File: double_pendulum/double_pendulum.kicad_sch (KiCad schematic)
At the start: 3 parts, among them J1 Conn_01x21_Socket, J2 Conn_01x21_Socket, U1 SC0915

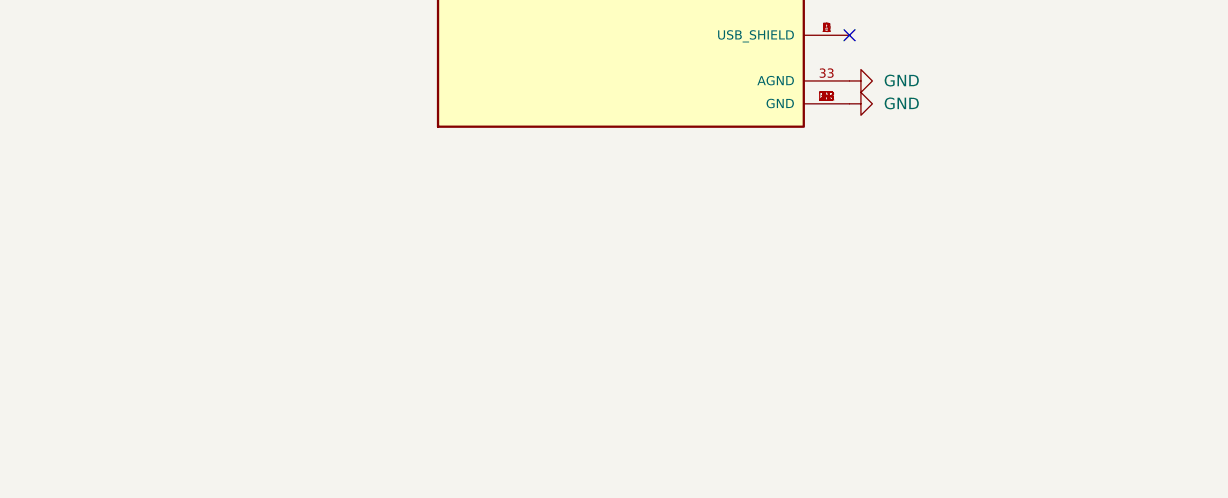
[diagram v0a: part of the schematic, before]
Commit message: Updated double pendulum with todo notes
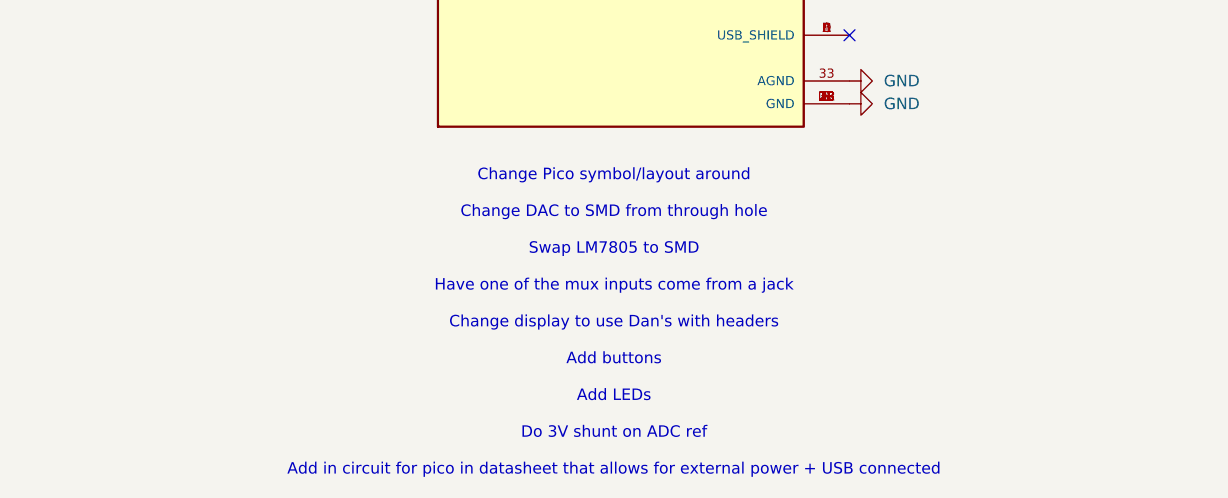
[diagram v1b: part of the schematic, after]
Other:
- note added: "Change Pico symbol/layout around Change DAC to SMD from through hole Swap LM7805 to SMD Have one of the mux inputs come from a jack Change display to use Dan's with headers Add buttons Add LEDs Do 3V shunt on ADC ref Add in circuit for pico in datasheet that allows for external power + USB connected"
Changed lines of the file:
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@@
 		(at 144.78 97.79)
+	)
+	(text "Change Pico symbol/layout around\n\nChange DAC to SMD from through hole\n\nSwap LM7805 to SMD\n\nHave one of the mux inputs come from a jack\n\nChange display to use Dan's with headers\n\nAdd buttons\n\nAdd LEDs\n\nDo 3V shunt on ADC ref\n\nAdd in circuit for pico in datasheet that allows for external power + USB connected "
+		(exclude_from_sim no)
+		(at 118.618 129.794 0)
+		(effects
+			(font
+				(size 1.27 1.27)
+			)
+		)
 	)
 	(global_label "SCL_DISPLAY"

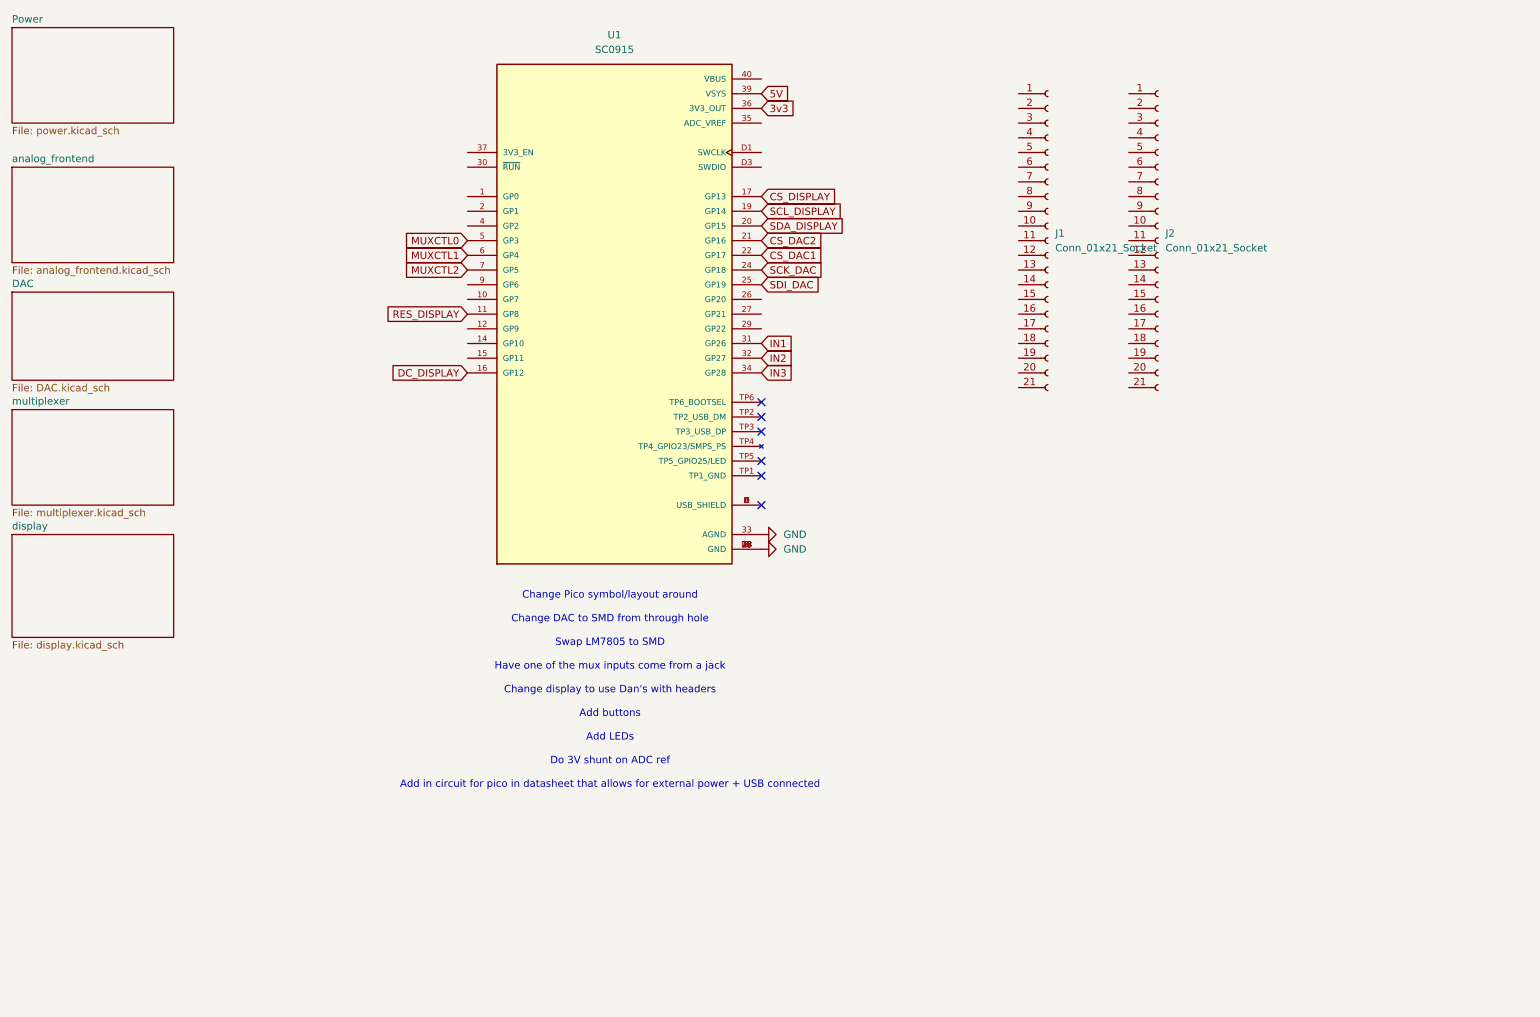
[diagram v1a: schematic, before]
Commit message: Finished schematic and layout of the double pendulum
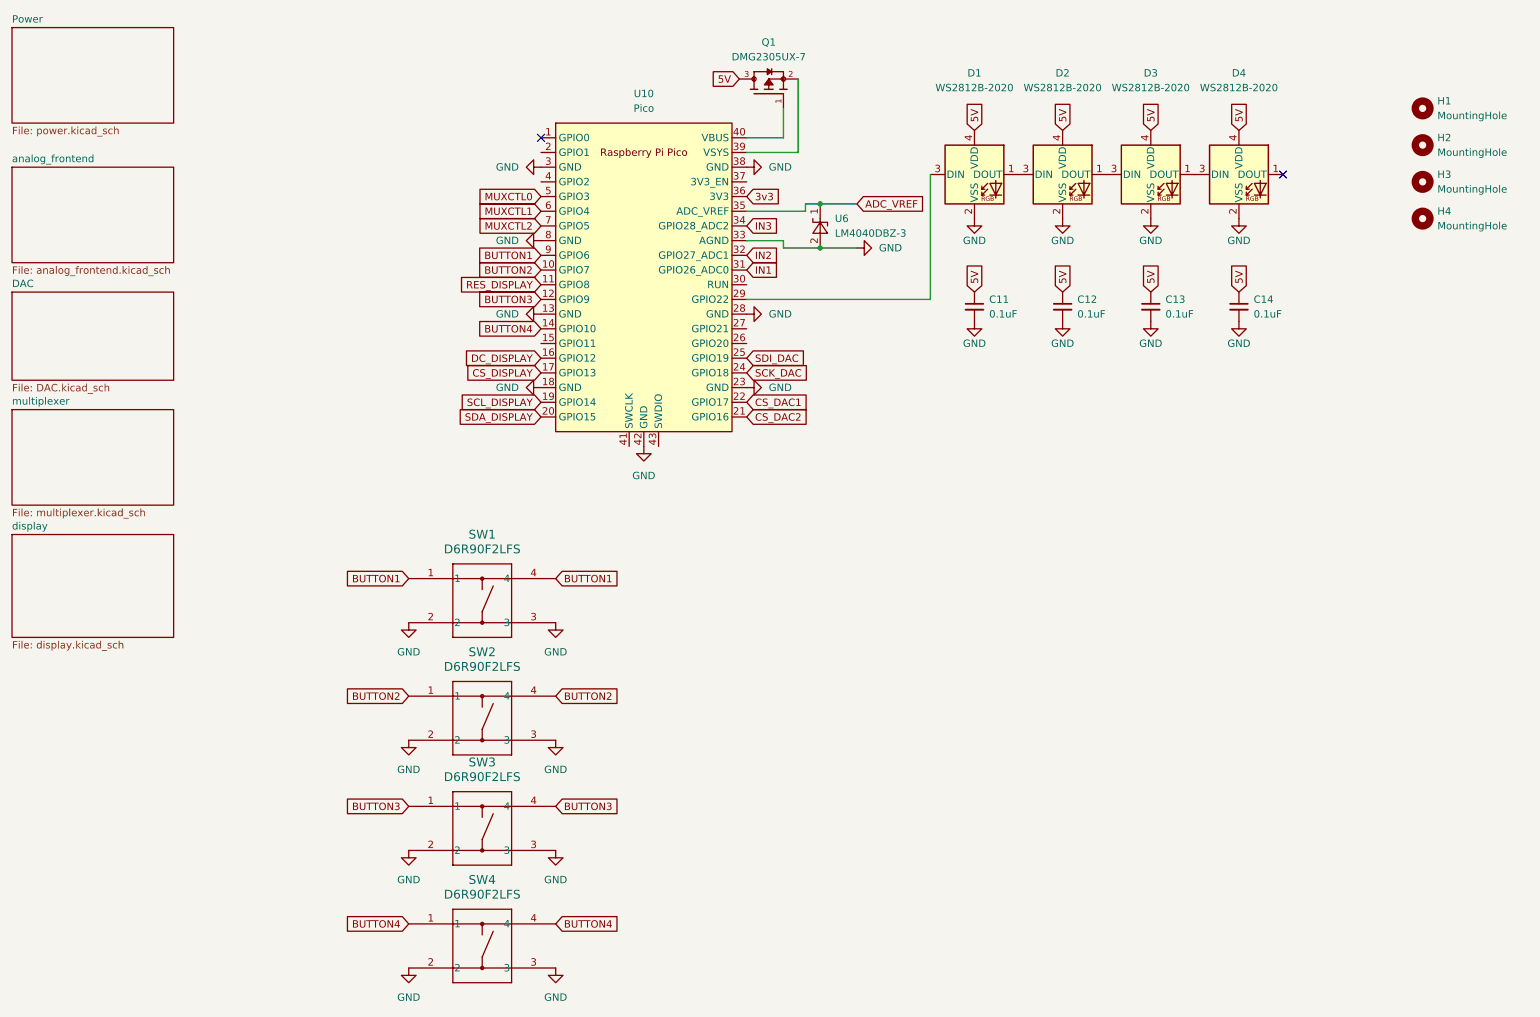
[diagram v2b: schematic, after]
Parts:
- removed J1, J2: Conn_01x21_Socket, Connector_PinHeader_2.54mm:PinHeader_1x20_P2.54mm_Vertical, symbol Connector:Conn_01x21_Socket
- removed U1: SC0915, SC0915:MODULE_SC0915, symbol SC0915:SC0915
- added C11, C12, C13, C14: 100nF_0402_16V, 4ms_Capacitor:C_0402, symbol 4ms_Capacitor:100nF_0402_16V
- added D1, D2, D3, D4: WS2812B-2020, LED_SMD:LED_WS2812B-2020_PLCC4_2.0x2.0mm, symbol LED:WS2812B-2020
- added H1, H2, H3, H4: MountingHole, 4ms_Faceplate:Faceplate_Rail_Mount_Slot_Plated, symbol Mechanical:MountingHole
- added Q1: DMG2305UX-7, DMG2305UX_7:SOT91P240X110-3N_DMG2305UX-7, symbol DMG2305UX-7:DMG2305UX-7
- added SW1, SW2, SW3, SW4: D6R90F2LFS, D6R90:D6R90_CNK, symbol D6R90:D6R90F2LFS
- added U10: Pico, MCU_RaspberryPi_and_Boards:RPi_Pico_SMD_TH, symbol MCU_RaspberryPi_and_Boards:Pico
- added U6: LM4040DBZ-3, Package_TO_SOT_SMD:SOT-23, symbol Reference_Voltage:LM4040DBZ-3
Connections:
- net 3v3: now also U10.36 (3V3)
- net 5V: now also C11.1, C12.1, C13.1, C14.1, D1.4 (VDD), D2.4 (VDD), D3.4 (VDD), D4.4 (VDD), Q1.3
- net CS_DAC1: now also U10.22 (GPIO17)
- net CS_DAC2: now also U10.21 (GPIO16)
- net CS_DISPLAY: now also U10.17 (GPIO13)
- net DC_DISPLAY: now also U10.16 (GPIO12)
- net GND: now also C11.2, C12.2, C13.2, C14.2, D1.2 (VSS), D2.2 (VSS), D3.2 (VSS), D4.2 (VSS), SW1.2, SW1.3, SW2.2, SW2.3, SW3.2, SW3.3, SW4.2, SW4.3, U10.13 (GND), U10.18 (GND), U10.23 (GND), U10.28 (GND), U10.3 (GND), U10.33 (AGND), U10.38 (GND), U10.42 (GND), U10.8 (GND), U6.2 (A)
- net IN1: now also U10.31 (GPIO26_ADC0)
- net IN2: now also U10.32 (GPIO27_ADC1)
- net IN3: now also U10.34 (GPIO28_ADC2)
- net MUXCTL0: now also U10.5 (GPIO3)
- net MUXCTL1: now also U10.6 (GPIO4)
- net MUXCTL2: now also U10.7 (GPIO5)
- net RES_DISPLAY: now also U10.11 (GPIO8)
- net SCK_DAC: now also U10.24 (GPIO18)
- net SCL_DISPLAY: now also U10.19 (GPIO14)
- net SDA_DISPLAY: now also U10.20 (GPIO15)
- net SDI_DAC: now also U10.25 (GPIO19)
- new net: Q1.1, U10.40 (VBUS)
- new net: Q1.2, U10.39 (VSYS)
- new net: D2.1 (DOUT), D3.3 (DIN)
- new net: D1.1 (DOUT), D2.3 (DIN)
- new net: D1.3 (DIN), U10.29 (GPIO22)
- new net: D3.1 (DOUT), D4.3 (DIN)
- new net ADC_VREF: U10.35 (ADC_VREF), U6.1 (K)
- new net BUTTON1: SW1.1, SW1.4, U10.9 (GPIO6)
- new net BUTTON2: SW2.1, SW2.4, U10.10 (GPIO7)
- new net BUTTON3: SW3.1, SW3.4, U10.12 (GPIO9)
- new net BUTTON4: SW4.1, SW4.4, U10.14 (GPIO10)
- no-connect marks 6 -> 2
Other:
- note removed: "Change Pico symbol/layout around Change DAC to SMD from through hole Swap LM7805 to SMD Have one of the mux inputs come from a jack Change display to use Dan's with headers Add buttons Add LEDs Do 3V shunt on ADC ref Add in circuit for pico in datasheet that allows for external power + USB connected"
